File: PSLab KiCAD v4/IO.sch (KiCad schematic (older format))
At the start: 71 parts, among them J5 Sin, P1 Power_Sources, Q1 MMBT3906, U10 TL082, U11 6S21, U12 6S21, U13 TL082, U16 TL082, U7 LM324, U8 TL082, U9 MCP4728

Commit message: Optimizing layout
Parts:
- C22, C23, C24, C25, C26, C27, C28, C29, C30, C31, C32, C34, C35, C36, C37, C38, C39, C40, C41, C7: footprint Capacitors_SMD:C_0201 -> Capacitors_SMD:C_0603
- C33, C43, C6: footprint Capacitors_SMD:C_0402 -> Capacitors_SMD:C_0603
- R14, R15, R16, R17, R18, R19, R20, R21, R22, R23, R24, R25, R26, R27, R28, R29, R30, R31, R32, R33, R34, R35, R36, R37, R38, R39, R40, R41, R42, R43, R44, R45, R46, R47: footprint Resistors_SMD:R_0201 -> Resistors_SMD:R_0603

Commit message: Added Gerber files
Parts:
- RV1: value 47K -> 100K
- TP1, TP2: footprint Measurement_Points:Measurement_Point_Square-SMD-Pad_Small -> Measurement_Points:Measurement_Point_Round-SMD-Pad_Small

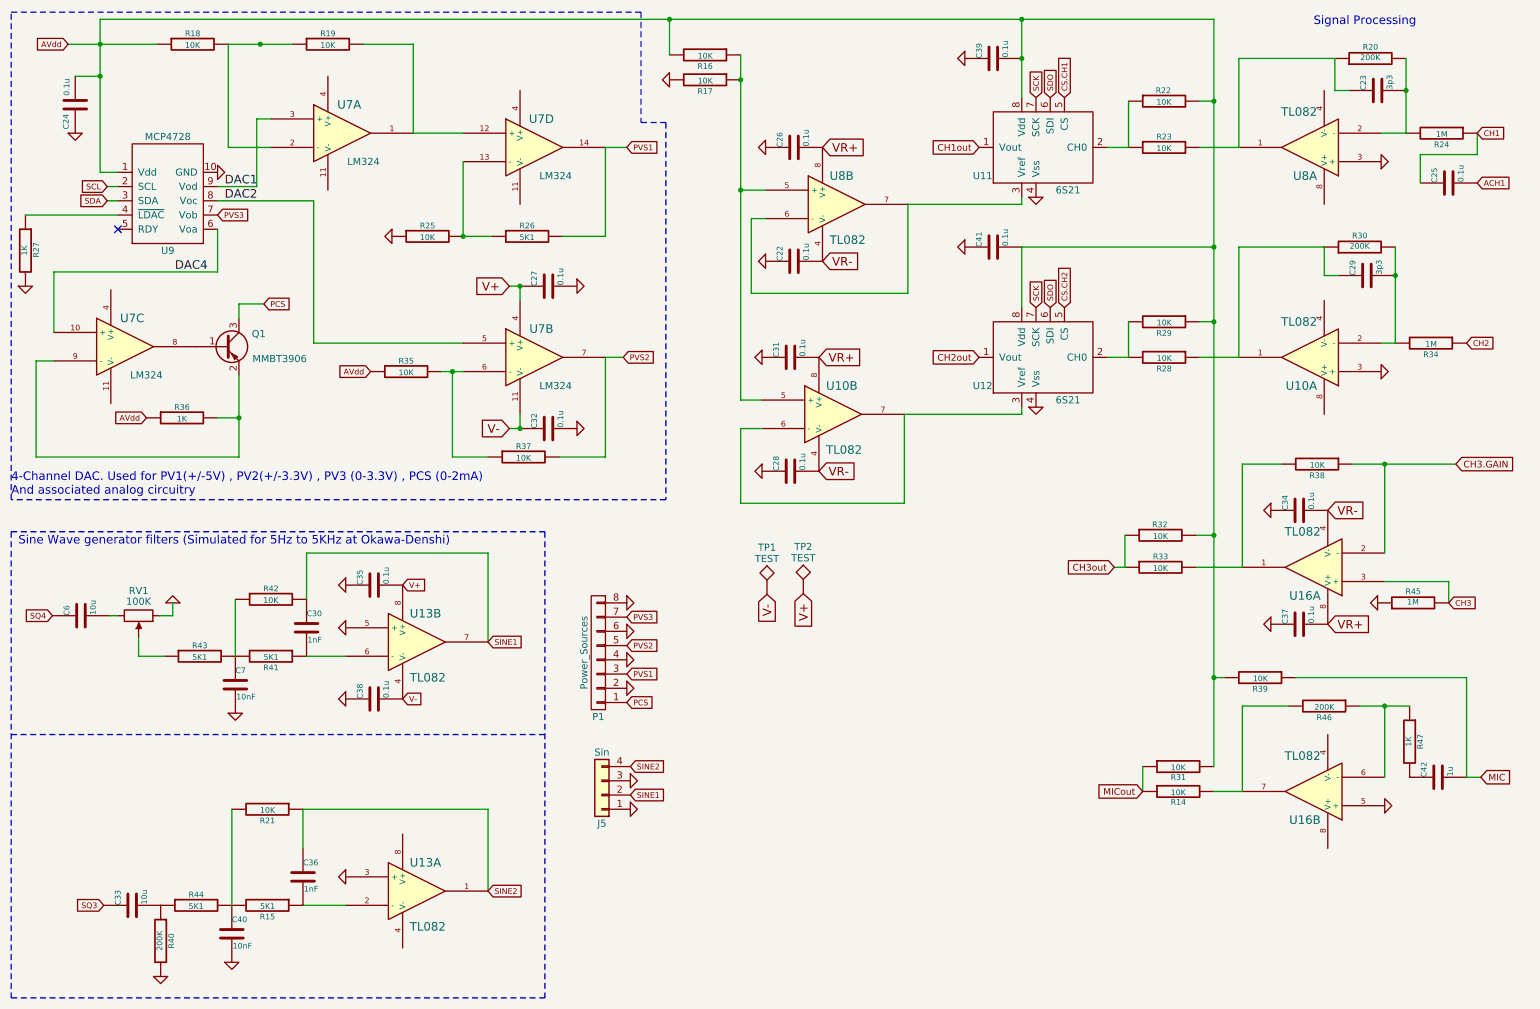
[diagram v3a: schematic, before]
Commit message: Updated docs with new layout
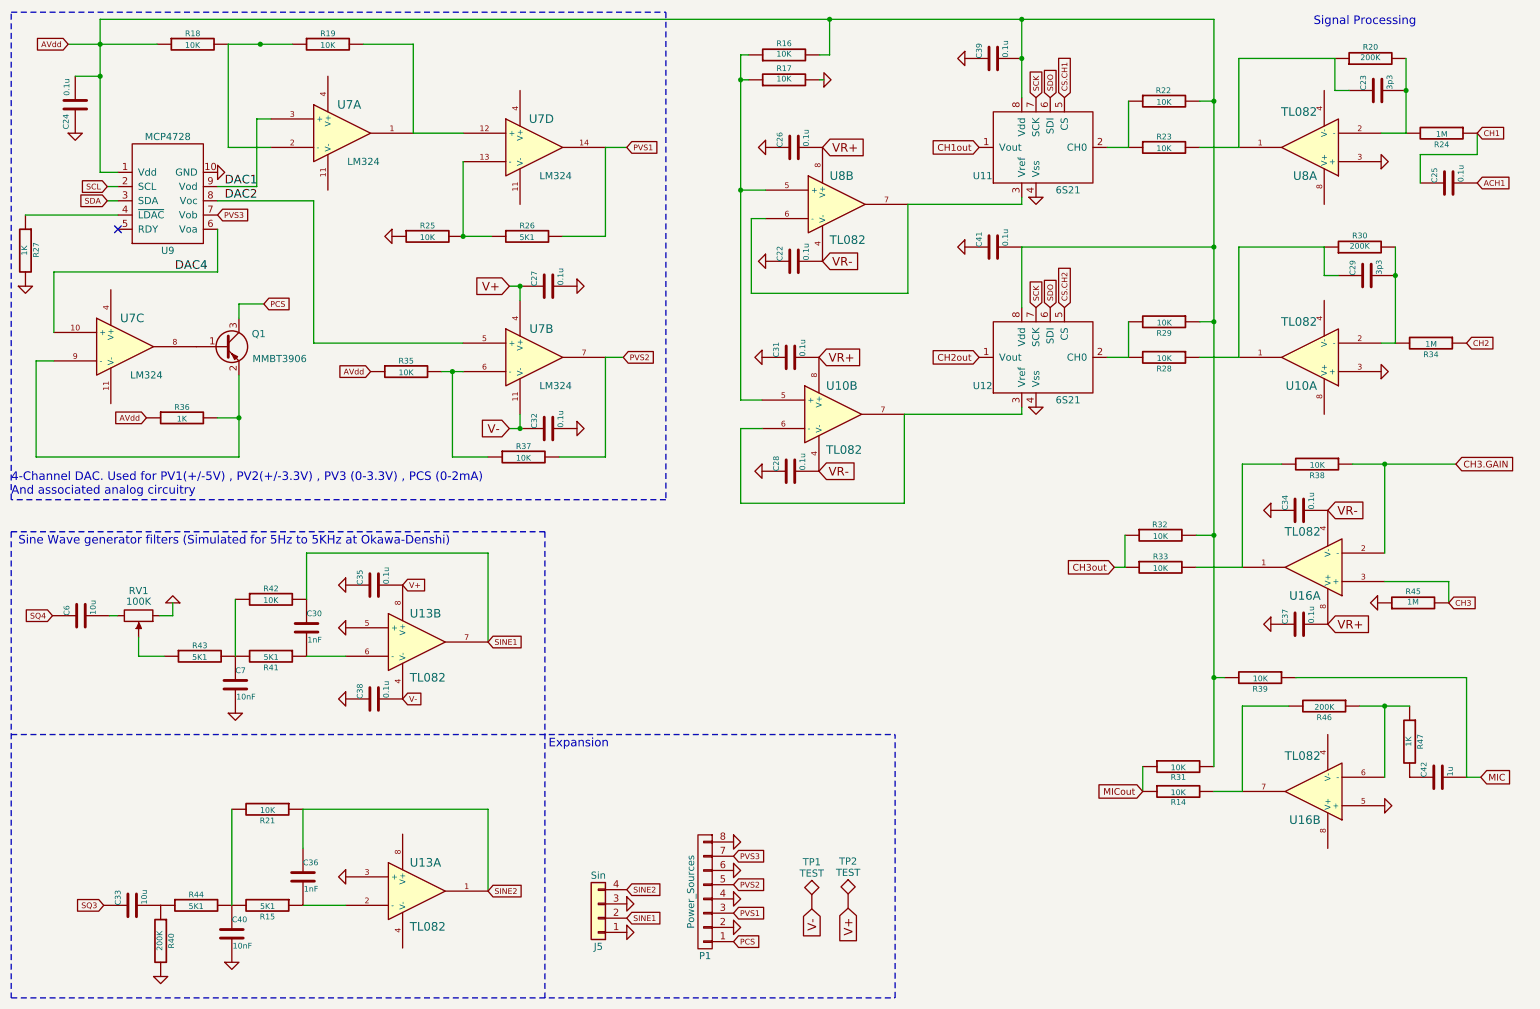
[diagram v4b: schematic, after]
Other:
- note added: "Expansion"
- moved on the sheet: J5, P1, R16, R17, TP1, TP2

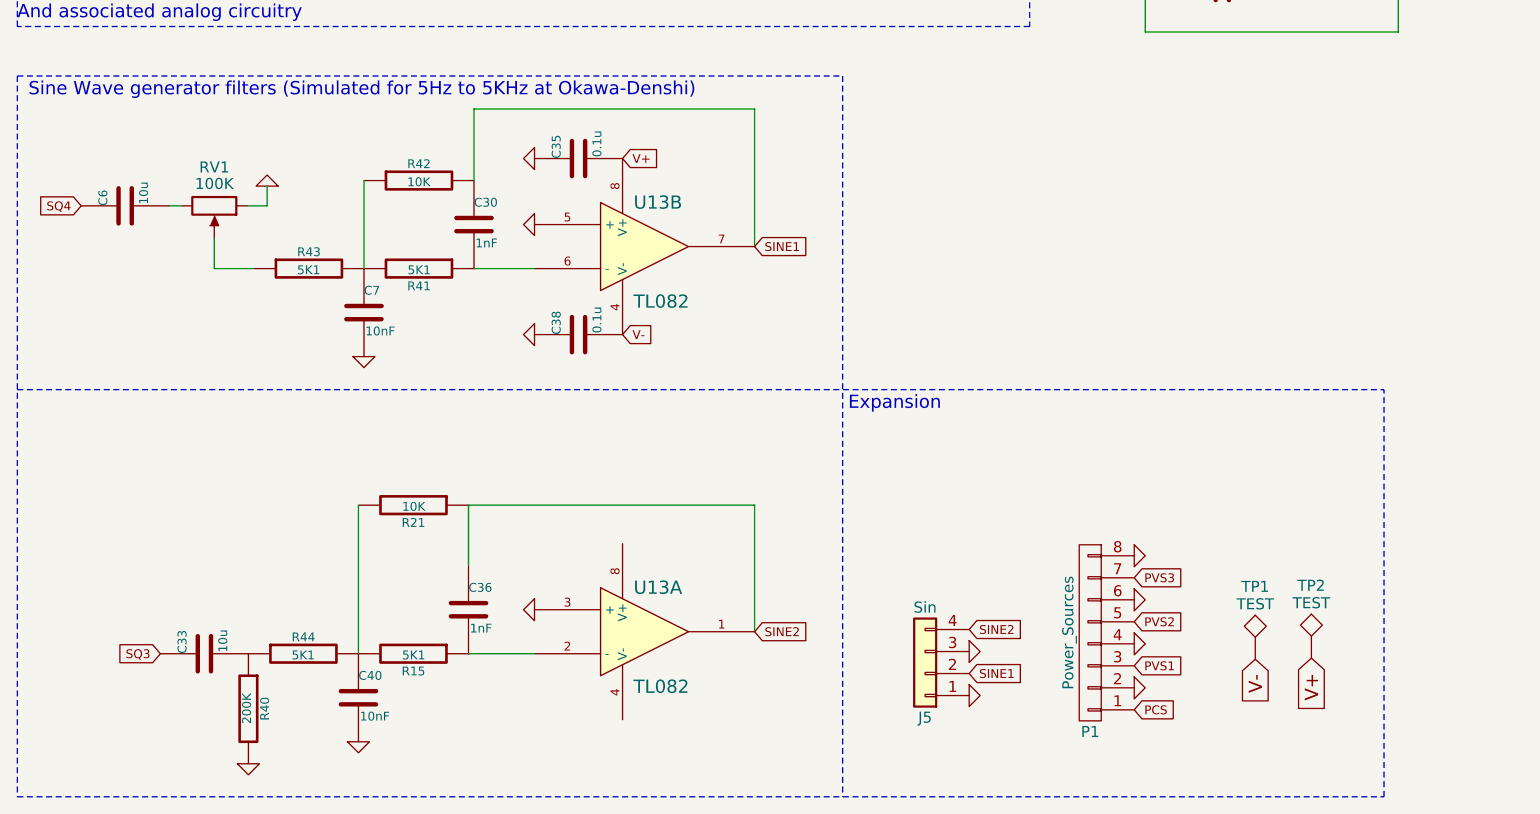
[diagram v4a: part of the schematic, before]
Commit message: New layout with pins adjusted + Bluetooth
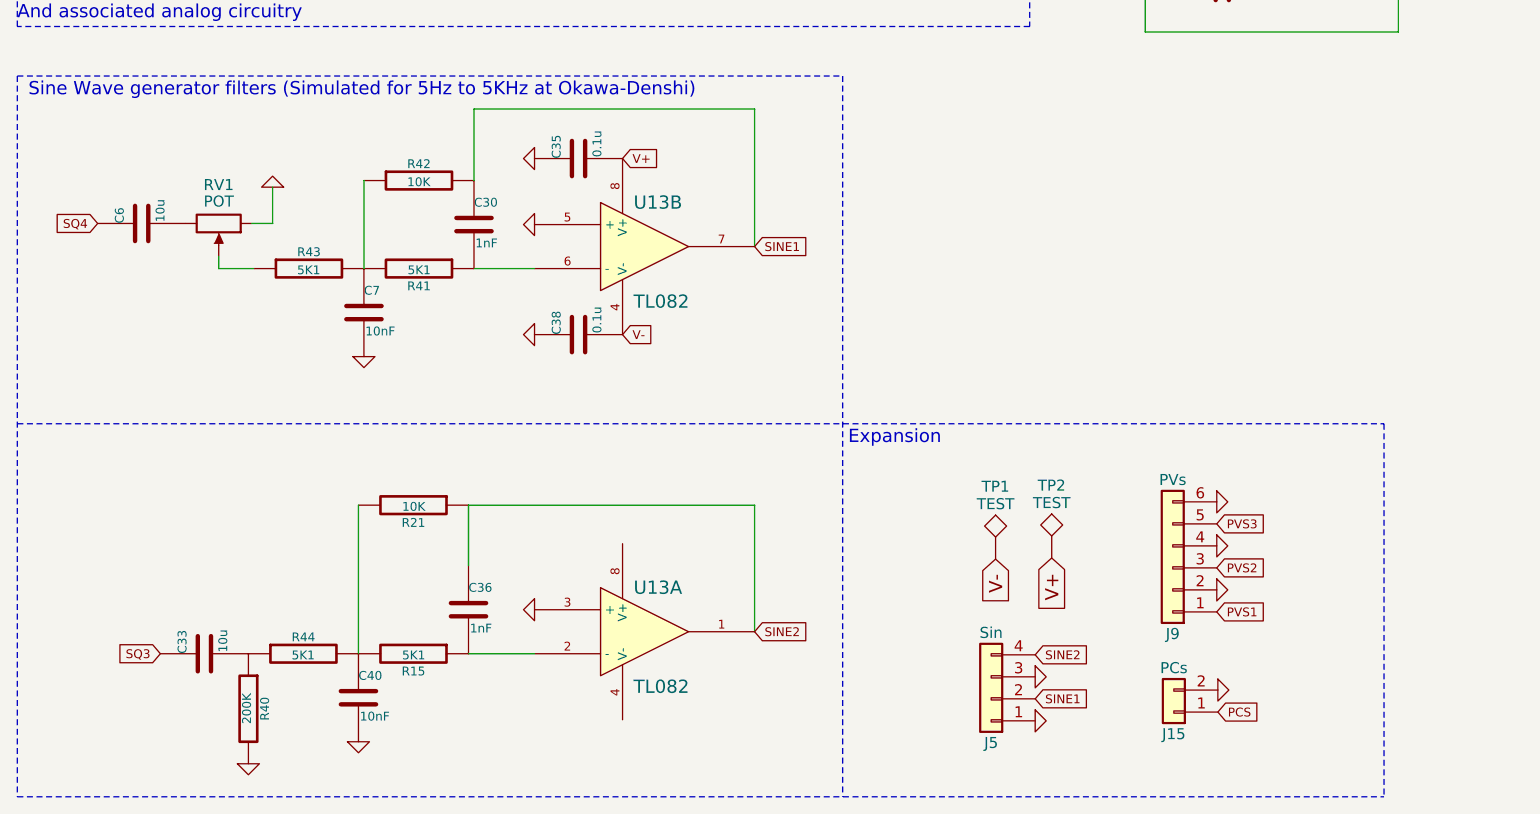
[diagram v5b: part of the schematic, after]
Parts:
- removed P1: Power_Sources, Pin_Headers:Pin_Header_Straight_1x08_Pitch2.54mm, symbol CONN_01X08
- added J15: PCs, Pin_Headers:Pin_Header_Straight_1x02_Pitch2.54mm, symbol Conn_01x02
- added J9: PVs, Pin_Headers:Pin_Header_Straight_1x06_Pitch2.54mm, symbol Conn_01x06
- RV1: value 100K -> POT
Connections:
- net GND: now also J15.2 (Pin_2), J9.2 (Pin_2), J9.4 (Pin_4), J9.6 (Pin_6)
- net PCS: now also J15.1 (Pin_1)
- net PVS1: now also J9.1 (Pin_1)
- net PVS2: now also J9.3 (Pin_3)
- net PVS3: now also J9.5 (Pin_5)
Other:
- moved on the sheet: C6, J5, TP1, TP2

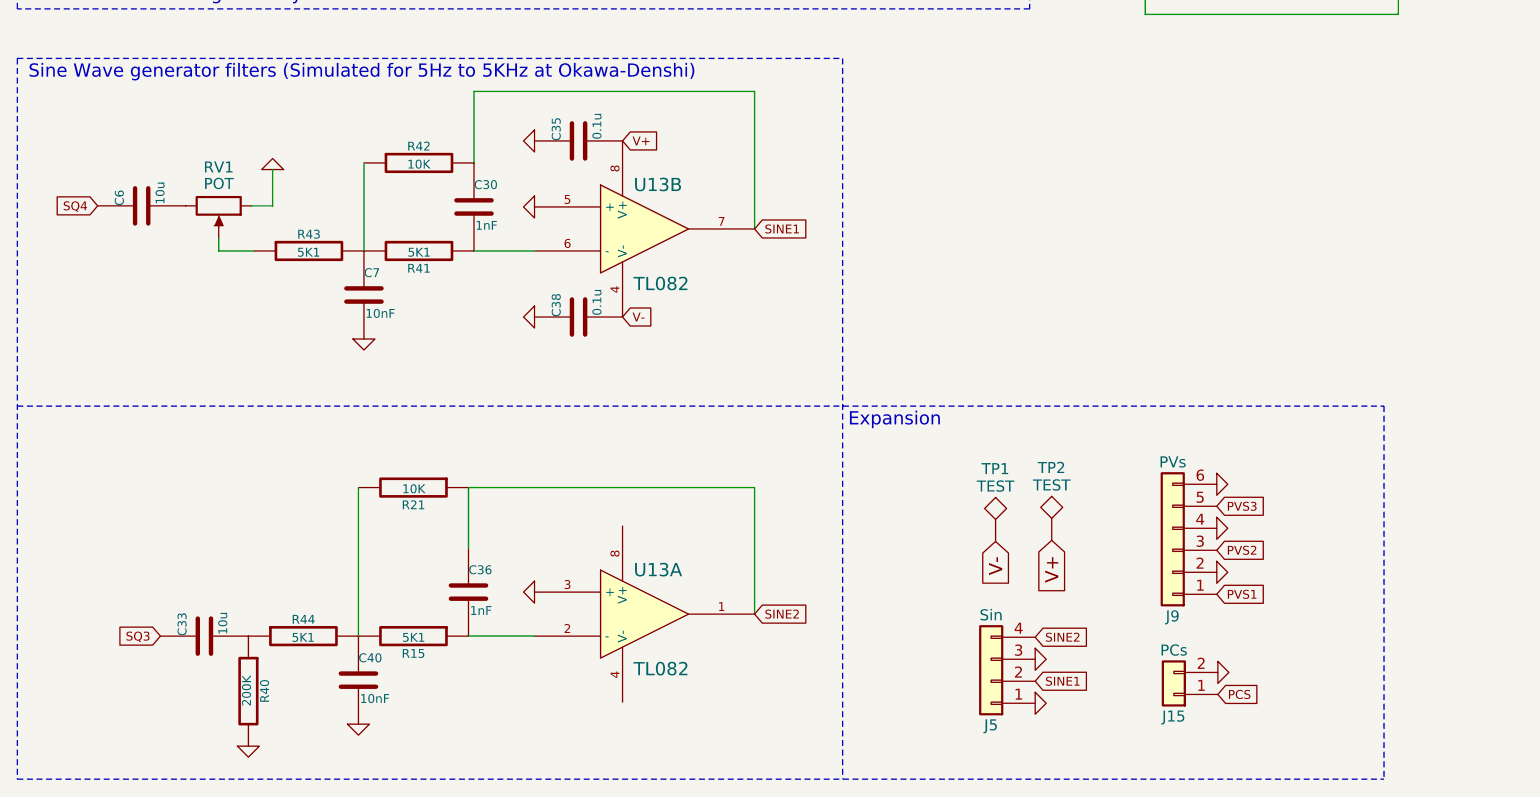
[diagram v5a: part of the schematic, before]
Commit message: Modifications to PSLab PCB (#39)
* Refined BOM Sheet

* Added FOSSASIA Logo and updated BoM

* NRF replaced with Bluetooth

* Modified silk screen texts
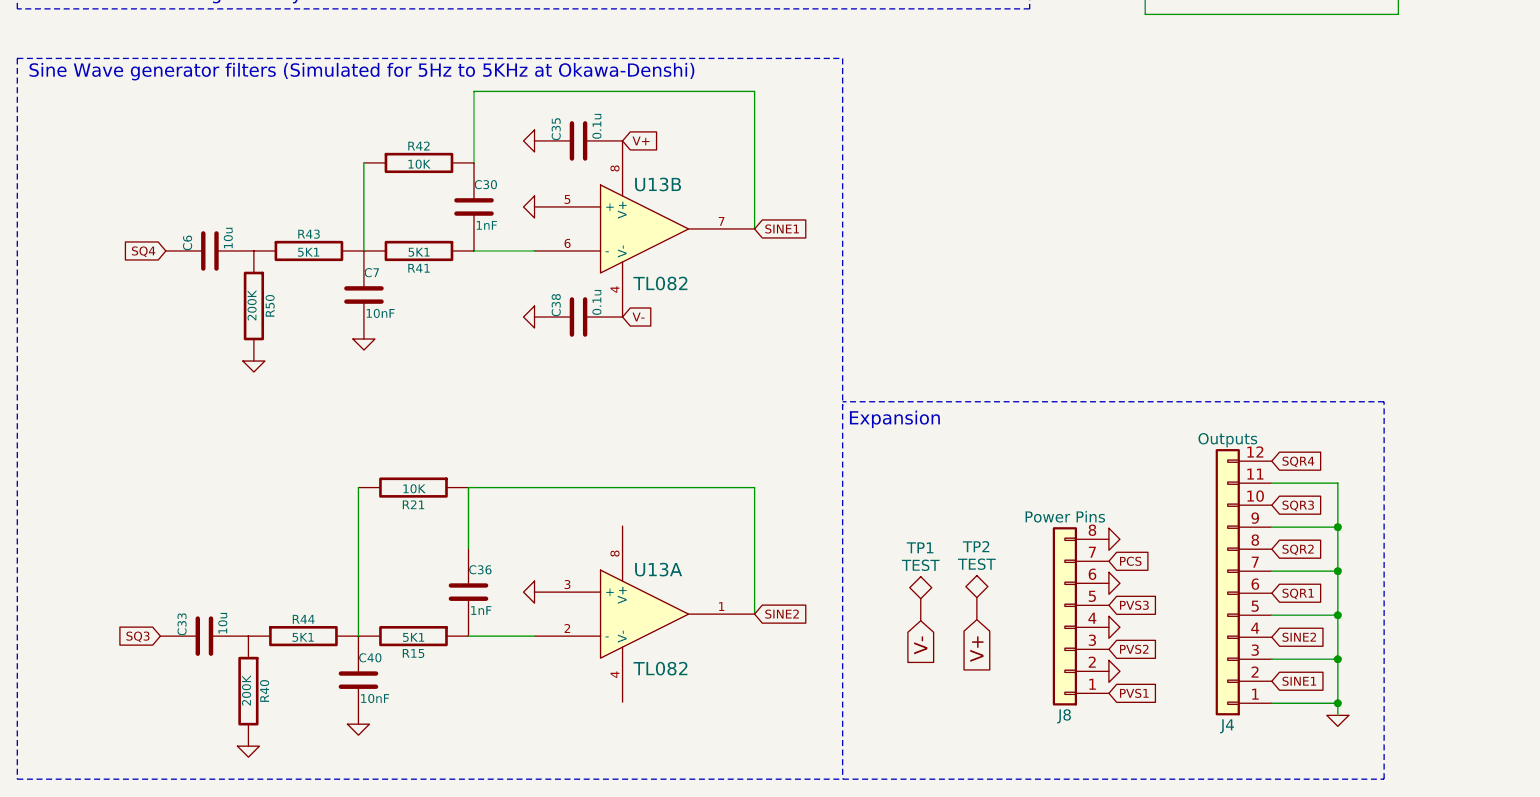
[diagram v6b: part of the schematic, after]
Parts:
- removed J15: PCs, Pin_Headers:Pin_Header_Straight_1x02_Pitch2.54mm, symbol Conn_01x02
- removed J5: Sin, Pin_Headers:Pin_Header_Straight_1x04_Pitch2.54mm, symbol Conn_01x04
- removed J9: PVs, Pin_Headers:Pin_Header_Straight_1x06_Pitch2.54mm, symbol Conn_01x06
- removed RV1: POT, Potentiometers:Potentiometer_Alps_RK09K_Vertical, symbol POT
- added J4: Outputs, Pin_Headers:Pin_Header_Straight_1x12_Pitch2.54mm, symbol Conn_01x12
- added J8: Power Pins, Pin_Headers:Pin_Header_Straight_1x08_Pitch2.54mm, symbol Conn_01x08
- added R50: 200K, Resistors_SMD:R_0603, symbol R-RESCUE-proto1
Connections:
- net GND: now also J4.1 (Pin_1), J4.11 (Pin_11), J4.3 (Pin_3), J4.5 (Pin_5), J4.7 (Pin_7), J4.9 (Pin_9), J8.2 (Pin_2), J8.4 (Pin_4), J8.6 (Pin_6), J8.8 (Pin_8), R50.2
- net PCS: now also J8.7 (Pin_7)
- net PVS1: now also J8.1 (Pin_1)
- net PVS2: now also J8.3 (Pin_3)
- net PVS3: now also J8.5 (Pin_5)
- net SINE1: now also J4.2 (Pin_2)
- net SINE2: now also J4.4 (Pin_4)
- net at C6.2: now also R43.1, R50.1
- new net SQR1: J4.6 (Pin_6)
- new net SQR2: J4.8 (Pin_8)
- new net SQR3: J4.10 (Pin_10)
- new net SQR4: J4.12 (Pin_12)
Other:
- moved on the sheet: C6, TP1, TP2
